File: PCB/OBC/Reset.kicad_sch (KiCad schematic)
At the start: 25 parts, among them U5 STM32F405RGTx

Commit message: bomkicad
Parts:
- R11: LCSC Part Name (none) -> C19679468
- R12, R13: LCSC Part Name (none) -> C19701189
- XTAL3: LCSC Part Name (none) -> C6942002
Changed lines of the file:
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@@
 			)
 		)
+		(property "LCSC Part Name" "C19701189"
+			(at 147.32 162.56 0)
+			(effects
+				(font
+					(size 1.27 1.27)
+				)
+			)
+		)
 		(pin "2"
 		)
@@
 			)
 		)
+		(property "LCSC Part Name" "C19679468"
+			(at 60.96 168.91 0)
+			(effects
+				(font
+					(size 1.27 1.27)
+				)
+			)
+		)
 		(pin "1"
 		)
@@
 			)
 		)
+		(property "LCSC Part Name" "C19701189"
+			(at 158.75 162.56 0)
+			(effects
+				(font
+					(size 1.27 1.27)
+				)
+			)
+		)
 		(pin "2"
 		)
@@
 			)
 		)
+		(property "LCSC Part Name" "C6942002"
+			(at 41.91 95.25 0)
+			(effects
+				(font
+					(size 1.27 1.27)
+				)
+			)
+		)

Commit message: Revert "Merge branch 'main' of https://github.com/HernanIbarra60/OBC-"
This reverts commit 45b73800fdf824c252c0947f7787583bb3814567, reversing
changes made to df5dc6ac9bf84d542dd85559211e3d40553a5f31.
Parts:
- added RESET1: Conn_01x05, Connector_PinHeader_2.54mm:PinHeader_1x05_P2.54mm_Vertical_SMD_Pin1Right, symbol Connector_Generic:Conn_01x05
- C35, C40, C43, C45, C46: LCSC Part Name C1591 -> C15725
- FB3: Mouser (none) -> 81-BLM21HE601SN1L
- R11: LCSC Part Name C19679468 -> C2907219; now in the parts list
- R12, R13: LCSC Part Name C19701189 -> C2930157; now in the parts list
- SwBoot3: LCSC Part Name C5962834 -> C22401620
- XTAL3: LCSC Part Name C6942002 -> (none); Mouser (none) -> 520-8012-30BQ-JES-TR
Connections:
- net SWD_NRST is gone; now on net SWDIO_RST: C45.1, SwReset3.2, U5.7 (NRST)
- net +3V3: now also RESET1.1 (Pin_1)
- net GND: now also RESET1.5 (Pin_5)
- net BOOT0 renamed BootRst
- net Rst_RX: no longer names the net of U5.14 (PA0)
- net Rst_RX: no longer U5.37 (PC6)
- net Rst_TX: no longer names the net of U5.15 (PA1)
- net Rst_TX: no longer U5.38 (PC7)
- net SWCLK3 renamed SWCLK_RST
- net SWCLK_RST: now also RESET1.2 (Pin_2)
- net SWDIO3 renamed SWDIO_RST
- net SWDIO_RST: now also RESET1.3 (Pin_3)
- new net MainPwr_RX: U5.37 (PC6)
- new net MainPwr_TX: U5.38 (PC7)
- new net SWNRST_RST: RESET1.4 (Pin_4)
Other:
- moved on the sheet: C33, C36, C38, C39, D6, D7, FB3, R12, R13, XTAL3

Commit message: Finishing schematics
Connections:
- net LGreen is gone; now on net LGreenP: R13.1
- net LRed is gone; now on net LRedP: R12.1
- net SWDIO_RST: no longer C45.1, SwReset3.2, U5.7 (NRST)
- net LGreenP: now reaches U5.14 (PA0)
- net LRedP: now reaches U5.15 (PA1)
- net watchdog: now reaches U5.22 (PA6)
- net MainRst: now reaches U5.33 (PB12)
- net ComsRst: now reaches U5.35 (PB14)
- net EN_ADCS_5V: now reaches U5.50 (PA15)
- net SWNRST_RST renamed SWD_NRST
- net SWD_NRST: now also C45.1, SwReset3.2, U5.7 (NRST)
- net set_0: no longer names the net of U5.23 (PA7)
- net set_1: no longer names the net of U5.24 (PC4)
- net set_2: no longer names the net of U5.25 (PC5)
- no-connect marks 36 -> 35
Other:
- moved on the sheet: C45, D6, D7, R12, R13, SwReset3

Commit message: Add some netclasses
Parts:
- added D8: D_Schottky, Diode_SMD:D_SOD-323_HandSoldering, symbol Device:D_Schottky
- C37, C41: footprint Capacitor_SMD:C_0805_2012Metric_Pad1.18x1.45mm_HandSolder -> Capacitor_SMD:C_0603_1608Metric_Pad1.08x0.95mm_HandSolder; LCSC Part Name C1711 -> C15725
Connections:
- net +3V3: now also D8.1 (K); no longer RESET1.1 (Pin_1)
- new net: D8.2 (A), RESET1.1 (Pin_1)
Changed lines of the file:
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@@
 	(paper "A4")
 	(rectangle
-		(start 35.56 152.4)
-		(end 127 186.69)
+		(start 127 152.4)
+		(end 168.91 186.69)
 		(stroke
 			(width 0)
@@
 		)
 	)
-	(text "Boot and Reset "
-		(exclude_from_sim no)
-		(at 77.978 151.13 0)
-		(effects
-			(font
-				(size 1.27 1.27)
-				(thickness 0.254)
-				(bold yes)
-			)
+	(rectangle
+		(start 35.56 152.4)
+		(end 127 186.69)
+		(stroke
+			(width 0)
+			(type default)
+		)
+		(fill
+			(type none)
 		)
 	)
-	(text_box ""
-		(exclude_from_sim no)
-		(at 127 152.4 0)
-		(size 43.18 34.29)
-		(margins 0.9525 0.9525 0.9525 0.9525)
+	(rectangle
+		(start 127 152.4)
+		(end 127 186.69)
 		(stroke
 			(width 0)
-			(type solid)
+			(type default)
 		)
 		(fill
 			(type none)
 		)
+	)
+	(text "Boot and Reset "
+		(exclude_from_sim no)
+		(at 77.978 151.13 0)
 		(effects
 			(font
 				(size 1.27 1.27)
+				(thickness 0.254)
+				(bold yes)
 			)
-			(justify left top)
 		)
 	)
@@
 	(wire
 		(pts
-			(xy 144.78 163.83) (xy 151.13 163.83)
+			(xy 40.64 171.45) (xy 43.18 171.45)
 		)
 		(stroke
@@
 	(wire
 		(pts
-			(xy 40.64 171.45) (xy 43.18 171.45)
+			(xy 86.36 25.4) (xy 97.79 25.4)
 		)
 		(stroke
@@
 	(wire
 		(pts
-			(xy 86.36 25.4) (xy 97.79 25.4)
+			(xy 130.81 33.02) (xy 128.27 33.02)
 		)
 		(stroke
@@
 	(wire
 		(pts
-			(xy 130.81 33.02) (xy 128.27 33.02)
+			(xy 64.77 168.91) (xy 68.58 168.91)
 		)
 		(stroke
@@
 	(wire
 		(pts
-			(xy 64.77 168.91) (xy 68.58 168.91)
+			(xy 52.07 54.61) (xy 52.07 57.15)
 		)
 		(stroke
@@
 	(wire
 		(pts
-			(xy 52.07 54.61) (xy 52.07 57.15)
+			(xy 120.65 33.02) (xy 123.19 33.02)
 		)
 		(stroke
@@
 	(wire
 		(pts
-			(xy 120.65 33.02) (xy 123.19 33.02)
+			(xy 54.61 83.82) (xy 60.96 83.82)
 		)
 		(stroke
@@
 	(wire
 		(pts
-			(xy 54.61 83.82) (xy 60.96 83.82)
+			(xy 137.16 161.29) (xy 137.16 158.75)
 		)
 		(stroke
@@
 	(wire
 		(pts
+			(xy 140.97 161.29) (xy 137.16 161.29)
+		)
+		(stroke
+			(width 0)
+			(type default)
+		)
+	)
+	(wire
+		(pts
 			(xy 149.86 33.02) (xy 160.02 33.02)
 		)
@@
 	(wire
 		(pts
+			(xy 148.59 161.29) (xy 151.13 161.29)
+		)
+		(stroke
+			(width 0)
+			(type default)
+		)
+	)
+	(wire
+		(pts
 			(xy 33.02 57.15) (xy 36.83 57.15)
 		)
@@
 		)
 	)
+	(wire
+		(pts
+			(xy 151.13 161.29) (xy 151.13 163.83)
+		)
+		(stroke
+			(width 0)
+			(type default)
+		)
+	)
 	(label "SWCLK_RST"
 		(at 152.4 77.47 0)
@@
 			)
 		)
-		(property "Footprint" "Capacitor_SMD:C_0805_2012Metric_Pad1.18x1.45mm_HandSolder"
+		(property "Footprint" "Capacitor_SMD:C_0603_1608Metric_Pad1.08x0.95mm_HandSolder"
 			(at 87.3252 33.02 0)
 			(effects
@@
 			)
 		)
-		(property "LCSC Part Name" "C1711"
+		(property "LCSC Part Name" "C15725"
 			(at 86.36 29.21 0)
 			(effects
@@
 	)
 	(symbol
+		(lib_id "Device:D_Schottky")
+		(at 144.78 161.29 0)
+		(unit 1)
+		(exclude_from_sim no)
+		(in_bom yes)
+		(on_board yes)
+		(dnp no)
+		(fields_autoplaced yes)
+		(property "Reference" "D8"
+			(at 144.4625 154.94 0)
+			(effects
+				(font
+					(size 1.27 1.27)
+				)
+			)
+		)
+		(property "Value" "D_Schottky"
+			(at 144.4625 157.48 0)
+			(effects
+				(font
+					(size 1.27 1.27)
+				)
+			)
+		)
+		(property "Footprint" "Diode_SMD:D_SOD-323_HandSoldering"
+			(at 144.78 161.29 0)
+			(effects
+				(font
+					(size 1.27 1.27)
+				)
+				(hide yes)
+			)
+		)
+		(property "Datasheet" "~"
+			(at 144.78 161.29 0)
+			(effects
+				(font
+					(size 1.27 1.27)
+				)
+				(hide yes)
+			)
+		)
+		(property "Description" "Schottky diode"
+			(at 144.78 161.29 0)
+			(effects
+				(font
+					(size 1.27 1.27)
+				)
+				(hide yes)
+			)
+		)
+		(property "LCSC Part Name" "C124187"
+			(at 144.78 161.29 0)
+			(effects
+				(font
+					(size 1.27 1.27)
+				)
+				(hide yes)
+			)
+		)
+		(property "MAXIMUM_PACKAGE_HEIGHT" ""
+			(at 144.78 161.29 0)
+			(effects
+				(font
+					(size 1.27 1.27)
+				)
+				(hide yes)
+			)
+		)
+		(property "Availability" ""
+			(at 144.78 161.29 0)
+			(effects
+				(font
+					(size 1.27 1.27)
+				)
+				(hide yes)
+			)
+		)
+		(property "Check_prices" ""
+			(at 144.78 161.29 0)
+			(effects
+				(font
+					(size 1.27 1.27)
+				)
+				(hide yes)
+			)
+		)
+		(property "Description_1" ""
+			(at 144.78 161.29 0)
+			(effects
+				(font
+					(size 1.27 1.27)
+				)
+				(hide yes)
+			)
+		)
+		(property "MF" ""
+			(at 144.78 161.29 0)
+			(effects
+				(font
+					(size 1.27 1.27)
+				)
+				(hide yes)
+			)
+		)
+		(property "MP" ""
+			(at 144.78 161.29 0)
+			(effects
+				(font
+					(size 1.27 1.27)
+				)
+				(hide yes)
+			)
+		)
+		(property "Package" ""
+			(at 144.78 161.29 0)
+			(effects
+				(font
+					(size 1.27 1.27)
+				)
+				(hide yes)
+			)
+		)
+		(property "Price" ""
+			(at 144.78 161.29 0)
+			(effects
+				(font
+					(size 1.27 1.27)
+				)
+				(hide yes)
+			)
+		)
+		(property "SnapEDA_Link" ""
+			(at 144.78 161.29 0)
+			(effects
+				(font
+					(size 1.27 1.27)
+				)
+				(hide yes)
+			)
+		)
+		(property "Mouser" ""
+			(at 144.78 161.29 0)
+			(effects
+				(font
+					(size 1.27 1.27)
+				)
+				(hide yes)
+			)
+		)
+		(pin "1"
+		)
+		(pin "2"
+		)
+		(instances
+			(project "OBC"
+				(path "/e2c03eef-3b12-44a7-ba52-633d5337a24a/3a8974f9-75f5-4e68-8bec-e287a5028d56"
+					(reference "D8")
+					(unit 1)
+				)
+			)
+		)
+	)
+	(symbol
 		(lib_id "Device:C")
 		(at 45.72 60.96 180)
@@
 			)
 		)
-		(property "Footprint" "Capacitor_SMD:C_0805_2012Metric_Pad1.18x1.45mm_HandSolder"
+		(property "Footprint" "Capacitor_SMD:C_0603_1608Metric_Pad1.08x0.95mm_HandSolder"
 			(at 64.4652 33.02 0)
 			(effects
@@
 			)
 		)
-		(property "LCSC Part Name" "C1711"
+		(property "LCSC Part Name" "C15725"
 			(at 63.5 29.21 0)
 			(effects
@@
 	(symbol
 		(lib_id "power:+3V3")
-		(at 144.78 163.83 0)
+		(at 137.16 158.75 0)
 		(unit 1)
 		(exclude_from_sim no)
@@
 		(fields_autoplaced yes)
 		(property "Reference" "#PWR0107"
-			(at 144.78 167.64 0)
+			(at 137.16 162.56 0)
 			(effects
 				(font
@@
 		)
 		(property "Value" "+3V3"
-			(at 144.78 158.75 0)
+			(at 137.16 153.67 0)
 			(effects
 				(font
@@
 		)
 		(property "Footprint" ""
-			(at 144.78 163.83 0)
+			(at 137.16 158.75 0)
 			(effects
 				(font
@@
 		)
 		(property "Datasheet" ""
-			(at 144.78 163.83 0)
+			(at 137.16 158.75 0)
 			(effects
 				(font
@@
 		)
 		(property "Description" "Power symbol creates a global label with name \"+3V3\""
-			(at 144.78 163.83 0)
+			(at 137.16 158.75 0)
 			(effects
 				(font

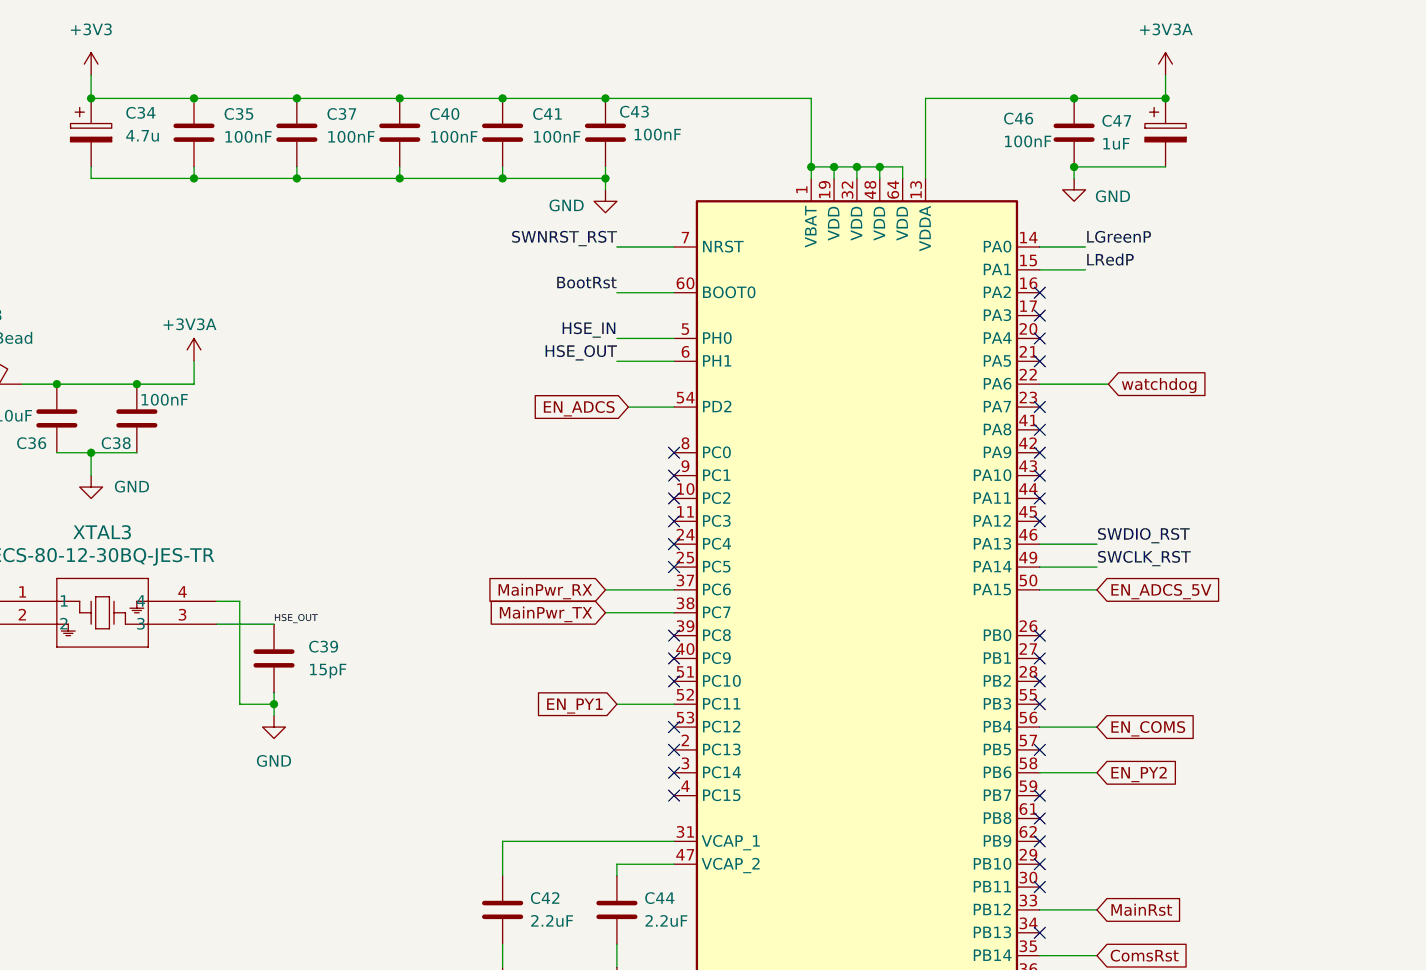
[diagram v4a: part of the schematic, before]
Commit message: Solo falta verificar el LDO
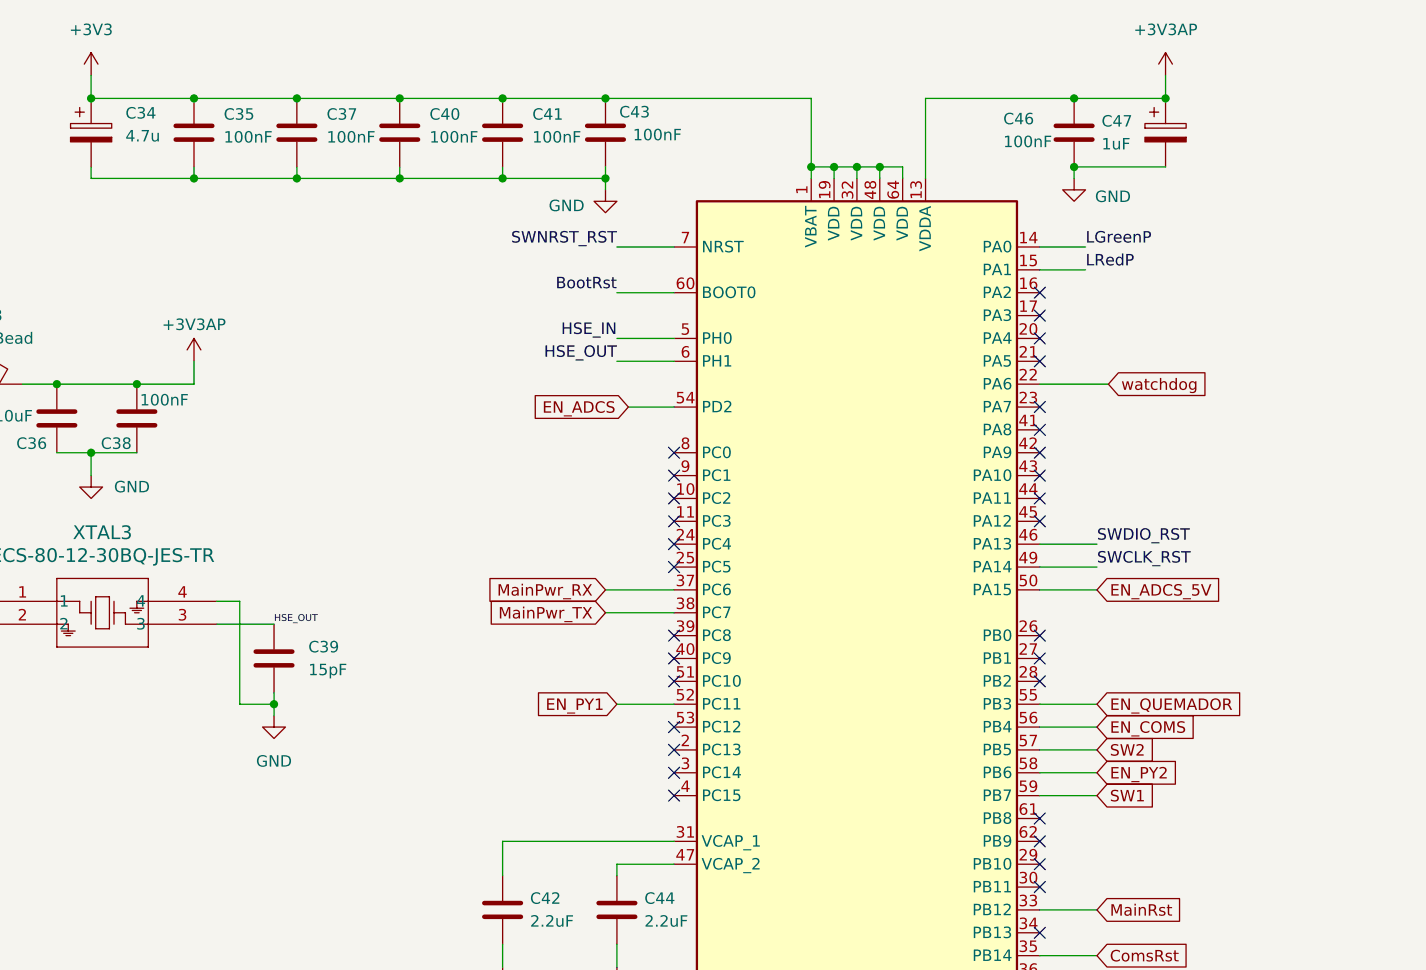
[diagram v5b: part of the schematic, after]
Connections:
- net EN_QUEMADOR: now reaches U5.55 (PB3)
- net SW2: now reaches U5.57 (PB5)
- net SW1: now reaches U5.59 (PB7)
- net +3V3A renamed +3V3AP
- no-connect marks 35 -> 32
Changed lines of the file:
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@@
-	)
-	(no_connect
-		(at 146.05 97.79)
-	)
-	(no_connect
-		(at 146.05 92.71)
 	)
 	(no_connect
@@
 	)
 	(no_connect
-		(at 146.05 102.87)
-	)
-	(no_connect
 		(at 146.05 54.61)
 	)
@@
 	(wire
 		(pts
+			(xy 146.05 97.79) (xy 152.4 97.79)
+		)
+		(stroke
+			(width 0)
+			(type default)
+		)
+	)
+	(wire
+		(pts
 			(xy 120.65 33.02) (xy 123.19 33.02)
 		)
@@
 	(wire
 		(pts
+			(xy 146.05 102.87) (xy 152.4 102.87)
+		)
+		(stroke
+			(width 0)
+			(type default)
+		)
+	)
+	(wire
+		(pts
 			(xy 63.5 34.29) (xy 52.07 34.29)
 		)
@@
 		(pts
 			(xy 102.87 171.45) (xy 102.87 173.99)
+		)
+		(stroke
+			(width 0)
+			(type default)
+		)
+	)
+	(wire
+		(pts
+			(xy 146.05 92.71) (xy 152.4 92.71)
 		)
 		(stroke
@@
 		)
 	)
+	(global_label "SW1"
+		(shape input)
+		(at 152.4 102.87 0)
+		(fields_autoplaced yes)
+		(effects
+			(font
+				(size 1.27 1.27)
+			)
+			(justify left)
+		)
+		(property "Intersheetrefs" "${INTERSHEET_REFS}"
+			(at 159.2556 102.87 0)
+			(effects
+				(font
+					(size 1.27 1.27)
+				)
+				(justify left)
+				(hide yes)
+			)
+		)
+	)
 	(global_label "EN_ADCS"
 		(shape input)
@@
 		)
 	)
+	(global_label "SW2"
+		(shape input)
+		(at 152.4 97.79 0)
+		(fields_autoplaced yes)
+		(effects
+			(font
+				(size 1.27 1.27)
+			)
+			(justify left)
+		)
+		(property "Intersheetrefs" "${INTERSHEET_REFS}"
+			(at 159.2556 97.79 0)
+			(effects
+				(font
+					(size 1.27 1.27)
+				)
+				(justify left)
+				(hide yes)
+			)
+		)
+	)
 	(global_label "MainRst"
 		(shape input)
@@
 		(property "Intersheetrefs" "${INTERSHEET_REFS}"
 			(at 162.7632 115.57 0)
+			(effects
+				(font
+					(size 1.27 1.27)
+				)
+				(justify left)
+				(hide yes)
+			)
+		)
+	)
+	(global_label "EN_QUEMADOR"
+		(shape input)
+		(at 152.4 92.71 0)
+		(fields_autoplaced yes)
+		(effects
+			(font
+				(size 1.27 1.27)
+			)
+			(justify left)
+		)
+		(property "Intersheetrefs" "${INTERSHEET_REFS}"
+			(at 169.0528 92.71 0)
 			(effects
 				(font
@@
 			)
 		)
-		(property "Value" "+3V3A"
+		(property "Value" "+3V3AP"
 			(at 160.02 17.78 0)
 			(effects
@@
 			)
 		)
-		(property "Value" "+3V3A"
+		(property "Value" "+3V3AP"
 			(at 48.514 50.546 0)
 			(effects
